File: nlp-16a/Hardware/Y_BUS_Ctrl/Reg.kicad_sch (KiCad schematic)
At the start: 4 parts

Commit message: YバスTMPRegリファレンス割り当て
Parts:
- gave numbers to parts that had none: 1
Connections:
- net Q: now also U16.10, U16.11; no longer U16.12, U16.8
- net at U16.3, U16.4: now also U16.12; no longer U16.9
- net at U16.6: now also U16.9; no longer U16.13
- new net: U16.13, U16.8
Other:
- moved on the sheet: U16C, U16D
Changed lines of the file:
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@@
   (symbol (lib_id "CD74HCXX:CD74HC00") (at 135.89 91.44 0) (unit 1)
     (in_bom yes) (on_board yes) (fields_autoplaced)
-    (property "Reference" "U?" (id 0) (at 135.89 82.55 0))
+    (property "Reference" "U16" (id 0) (at 135.89 82.55 0))
     (property "Value" "CD74HC00" (id 1) (at 135.89 85.09 0))
     (property "Footprint" "" (id 2) (at 130.81 91.44 0))
@@
   (symbol (lib_id "CD74HCXX:CD74HC00") (at 135.89 105.41 0) (unit 2)
     (in_bom yes) (on_board yes) (fields_autoplaced)
-    (property "Reference" "U?" (id 0) (at 135.89 96.52 0))
+    (property "Reference" "U16" (id 0) (at 135.89 96.52 0))
     (property "Value" "CD74HC00" (id 1) (at 135.89 99.06 0))
     (property "Footprint" "" (id 2) (at 130.81 105.41 0))
@@
     (pin "13")
   )
-  (symbol (lib_id "CD74HCXX:CD74HC00") (at 158.75 105.41 0) (unit 4)
+  (symbol (lib_id "CD74HCXX:CD74HC00") (at 158.75 91.44 0) (unit 4)
     (in_bom yes) (on_board yes) (fields_autoplaced)
-    (property "Reference" "U?" (id 0) (at 158.75 96.52 0))
-    (property "Value" "CD74HC00" (id 1) (at 158.75 99.06 0))
-    (property "Footprint" "" (id 2) (at 153.67 105.41 0))
-    (property "Datasheet" "" (id 3) (at 153.67 105.41 0))
+    (property "Reference" "U16" (id 0) (at 158.75 82.55 0))
+    (property "Value" "CD74HC00" (id 1) (at 158.75 85.09 0))
+    (property "Footprint" "" (id 2) (at 153.67 91.44 0))
+    (property "Datasheet" "" (id 3) (at 153.67 91.44 0))
     (pin "14")
     (pin "7")
@@
     (pin "13")
   )
-  (symbol (lib_id "CD74HCXX:CD74HC00") (at 158.75 91.44 0) (unit 3)
+  (symbol (lib_id "CD74HCXX:CD74HC00") (at 158.75 105.41 0) (mirror x) (unit 3)
     (in_bom yes) (on_board yes) (fields_autoplaced)
-    (property "Reference" "U?" (id 0) (at 158.75 82.55 0))
-    (property "Value" "CD74HC00" (id 1) (at 158.75 85.09 0))
-    (property "Footprint" "" (id 2) (at 153.67 91.44 0))
-    (property "Datasheet" "" (id 3) (at 153.67 91.44 0))
+    (property "Reference" "U16" (id 0) (at 158.75 96.52 0))
+    (property "Value" "CD74HC00" (id 1) (at 158.75 99.06 0))
+    (property "Footprint" "" (id 2) (at 153.67 105.41 0))
+    (property "Datasheet" "" (id 3) (at 153.67 105.41 0))
     (pin "14")
     (pin "7")

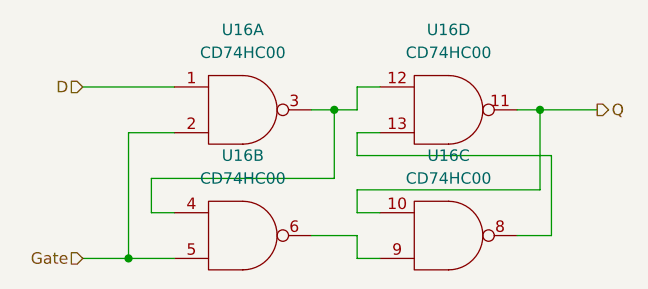
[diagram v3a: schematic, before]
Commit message: Yバス制御 配置の決定，リファレンスの割り当て，ERCの確認完了
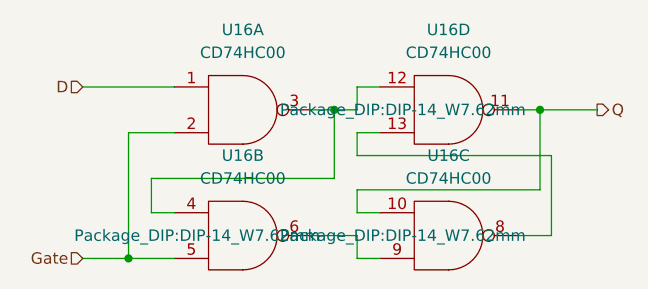
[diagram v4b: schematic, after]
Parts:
- U16: footprint (none) -> Package_DIP:DIP-14_W7.62mm
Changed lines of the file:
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@@
     (property "Reference" "U16" (id 0) (at 135.89 96.52 0))
     (property "Value" "CD74HC00" (id 1) (at 135.89 99.06 0))
-    (property "Footprint" "" (id 2) (at 130.81 105.41 0))
+    (property "Footprint" "Package_DIP:DIP-14_W7.62mm" (id 2) (at 130.81 105.41 0))
     (property "Datasheet" "" (id 3) (at 130.81 105.41 0))
     (pin "14")
@@
     (property "Reference" "U16" (id 0) (at 158.75 82.55 0))
     (property "Value" "CD74HC00" (id 1) (at 158.75 85.09 0))
-    (property "Footprint" "" (id 2) (at 153.67 91.44 0))
+    (property "Footprint" "Package_DIP:DIP-14_W7.62mm" (id 2) (at 153.67 91.44 0))
     (property "Datasheet" "" (id 3) (at 153.67 91.44 0))
     (pin "14")
@@
     (property "Reference" "U16" (id 0) (at 158.75 96.52 0))
     (property "Value" "CD74HC00" (id 1) (at 158.75 99.06 0))
-    (property "Footprint" "" (id 2) (at 153.67 105.41 0))
+    (property "Footprint" "Package_DIP:DIP-14_W7.62mm" (id 2) (at 153.67 105.41 0))
     (property "Datasheet" "" (id 3) (at 153.67 105.41 0))
     (pin "14")

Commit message: Y BUS制御の基板をとりあえず描いた．ビアとかはまた後で
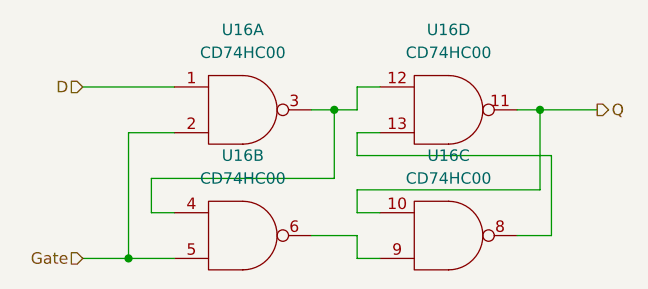
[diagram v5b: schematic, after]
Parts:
- U16: footprint (none) -> Package_DIP:DIP-14_W7.62mm
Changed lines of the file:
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@@
     (property "Reference" "U16" (id 0) (at 135.89 82.55 0))
     (property "Value" "CD74HC00" (id 1) (at 135.89 85.09 0))
-    (property "Footprint" "" (id 2) (at 130.81 91.44 0))
+    (property "Footprint" "Package_DIP:DIP-14_W7.62mm" (id 2) (at 130.81 91.44 0)
+      (effects (font (size 1.27 1.27)) hide)
+    )
     (property "Datasheet" "" (id 3) (at 130.81 91.44 0))
     (pin "14")
@@
     (property "Reference" "U16" (id 0) (at 135.89 96.52 0))
     (property "Value" "CD74HC00" (id 1) (at 135.89 99.06 0))
-    (property "Footprint" "Package_DIP:DIP-14_W7.62mm" (id 2) (at 130.81 105.41 0))
+    (property "Footprint" "Package_DIP:DIP-14_W7.62mm" (id 2) (at 130.81 105.41 0)
+      (effects (font (size 1.27 1.27)) hide)
+    )
     (property "Datasheet" "" (id 3) (at 130.81 105.41 0))
     (pin "14")
@@
     (property "Reference" "U16" (id 0) (at 158.75 82.55 0))
     (property "Value" "CD74HC00" (id 1) (at 158.75 85.09 0))
-    (property "Footprint" "Package_DIP:DIP-14_W7.62mm" (id 2) (at 153.67 91.44 0))
+    (property "Footprint" "Package_DIP:DIP-14_W7.62mm" (id 2) (at 153.67 91.44 0)
+      (effects (font (size 1.27 1.27)) hide)
+    )
     (property "Datasheet" "" (id 3) (at 153.67 91.44 0))
     (pin "14")
@@
   )
   (symbol (lib_id "CD74HCXX:CD74HC00") (at 158.75 105.41 0) (mirror x) (unit 3)
-    (in_bom yes) (on_board yes) (fields_autoplaced)
+    (in_bom yes) (on_board yes)
     (property "Reference" "U16" (id 0) (at 158.75 96.52 0))
     (property "Value" "CD74HC00" (id 1) (at 158.75 99.06 0))
-    (property "Footprint" "Package_DIP:DIP-14_W7.62mm" (id 2) (at 153.67 105.41 0))
+    (property "Footprint" "Package_DIP:DIP-14_W7.62mm" (id 2) (at 153.67 105.41 0)
+      (effects (font (size 1.27 1.27)) hide)
+    )
     (property "Datasheet" "" (id 3) (at 153.67 105.41 0))
     (pin "14")
